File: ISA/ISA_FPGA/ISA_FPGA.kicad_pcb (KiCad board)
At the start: 2 copper layers, 44 parts, among them J1 Bus_ISA_16bit, J2 DE15, P1 CONN_5X2, P2 14.31818MHz, U1 74LVC245, U2 74LVC245, U3 74LVC245, U4 74LVC245, U5 74LVC245, U6 74LVC245, U7 CONN_30X2, U8 CONN_30X2, U9 74LVC06, X1 MINI_DIN_6, X2 MINI_DIN_6

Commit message: ISA - FPGA board
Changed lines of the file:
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@@
   (general
     (thickness 1.6)
-    (drawings 11)
+    (drawings 19)
     (tracks 0)
     (zones 0)
@@
       (net 79 /GND))
   )
+  (gr_line (start 274.828 32.766) (end 275.082 32.766) (layer F.SilkS) (width 0.12))
+  (gr_line (start 275.082 32.766) (end 275.082 32.766) (layer F.SilkS) (width 0.12))
+  (gr_line (start 88.646 32.512) (end 88.646 33.274) (layer F.SilkS) (width 0.12))
+  (gr_line (start 88.646 32.512) (end 88.646 32.512) (layer F.SilkS) (width 0.12))
+  (gr_line (start 88.9 152.4) (end 88.646 33.274) (layer F.SilkS) (width 0.12))
+  (gr_line (start 88.9 152.146) (end 105.664 152.146) (layer F.SilkS) (width 0.12))
+  (gr_line (start 105.41 152.146) (end 88.9 152.146) (layer F.SilkS) (width 0.12))
+  (gr_line (start 88.392 32.512) (end 88.646 33.02) (layer F.SilkS) (width 0.12))
+  (gr_line (start 274.828 32.766) (end 88.646 32.512) (layer F.SilkS) (width 0.12))
+  (gr_line (start 14.732 33.274) (end 14.224 33.274) (layer F.SilkS) (width 0.12))
+  (gr_line (start 88.9 152.4) (end 88.9 152.4) (layer F.SilkS) (width 0.12))
   (dimension 60.96 (width 0.12) (layer F.SilkS)
     (gr_text "60.960 mm" (at 172.72 39.37) (layer F.SilkS)
@@
     (arrow2b (pts (xy 203.2 38.1) (xy 202.073496 38.686421)))
   )
-  (gr_line (start 275.082 33.02) (end 14.224 33.274) (layer F.SilkS) (width 0.12))
-  (gr_line (start 14.478 152.4) (end 14.224 32.512) (layer F.SilkS) (width 0.12))
-  (gr_line (start 105.664 152.146) (end 14.478 152.4) (layer F.SilkS) (width 0.12))
   (gr_line (start 105.664 143.51) (end 105.664 152.146) (layer F.SilkS) (width 0.12))
   (gr_line (start 117.602 143.51) (end 105.664 143.51) (layer F.SilkS) (width 0.12))

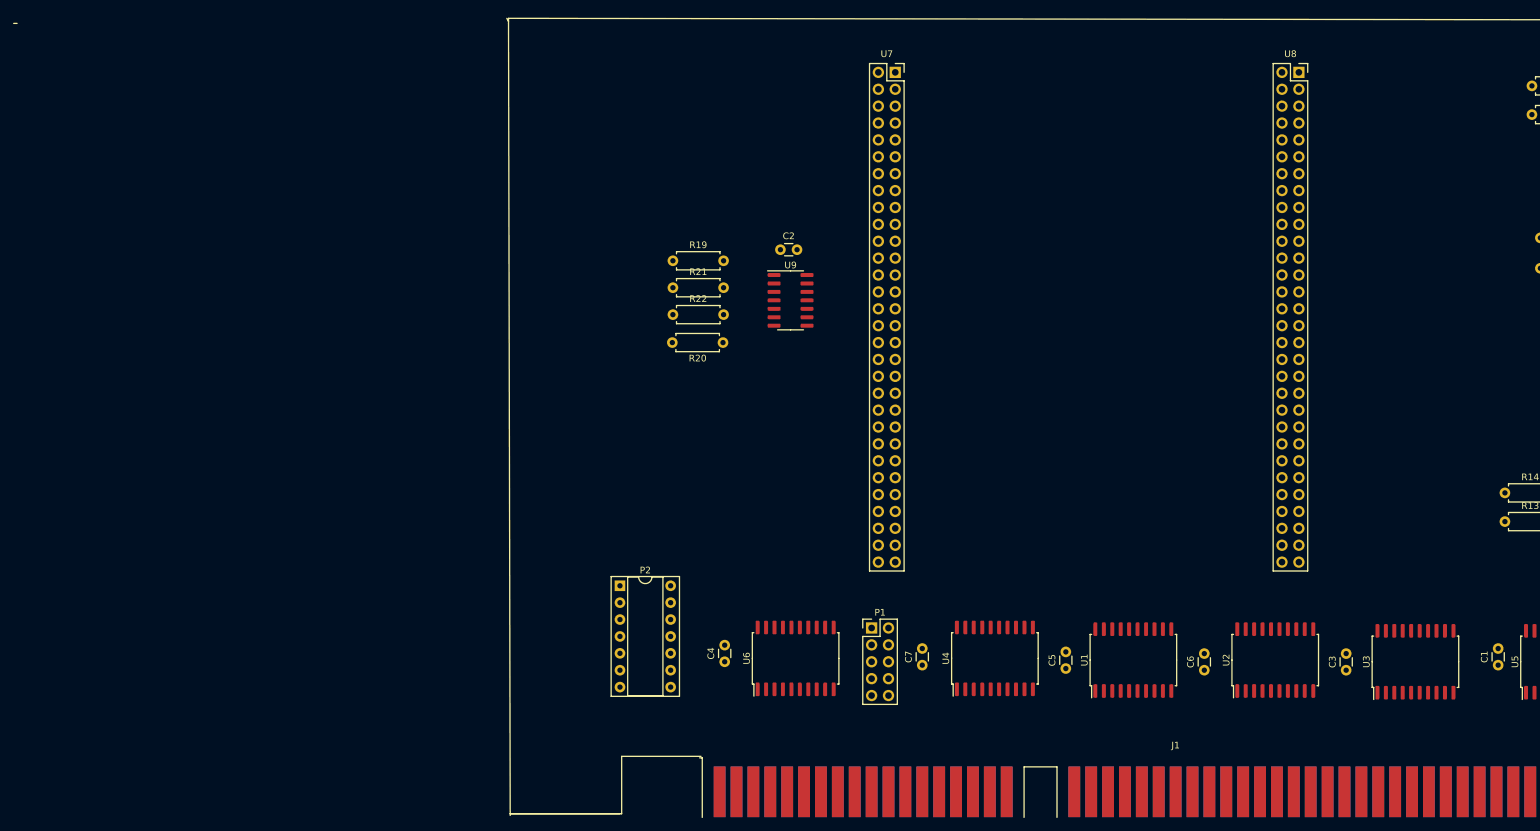
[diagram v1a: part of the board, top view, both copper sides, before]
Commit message: ISA - update
cad files for ISA video / cpu boards
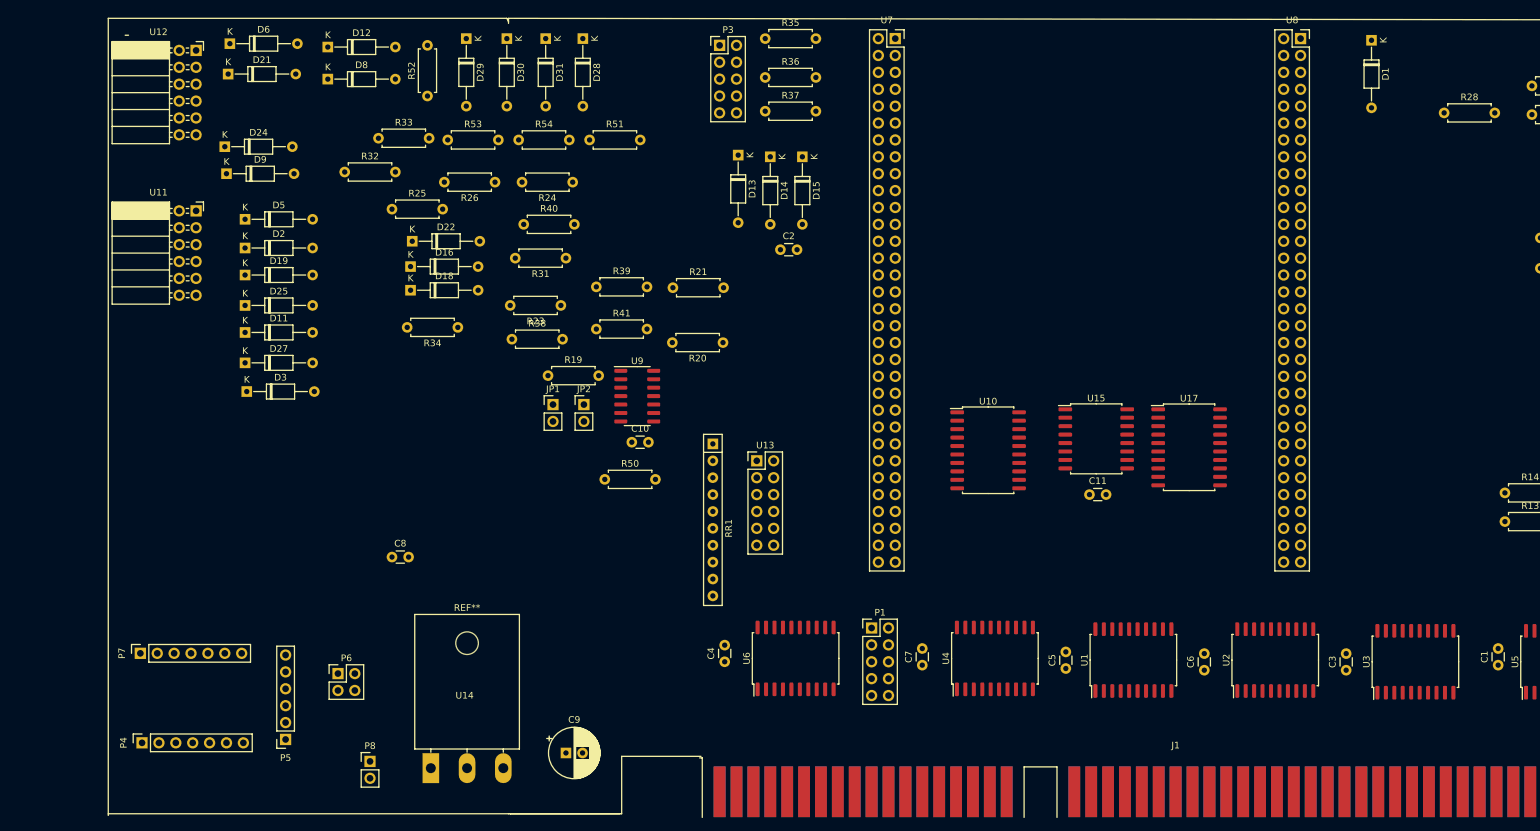
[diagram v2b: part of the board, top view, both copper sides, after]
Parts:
- removed P2: 14.31818MHz, Package_DIP:DIP-14_W7.62mm_Socket
- removed R22: 2k2, Resistor_THT:R_Axial_DIN0207_L6.3mm_D2.5mm_P7.62mm_Horizontal
- added C10: 0.1, Capacitor_THT:C_Disc_D3.0mm_W1.6mm_P2.50mm, F.Cu at (107.2, 96.3)
- added C11: 0.1, Capacitor_THT:C_Disc_D3.0mm_W1.6mm_P2.50mm, F.Cu at (176.0, 104.1)
- added C8: 0.1, Capacitor_THT:C_Disc_D3.0mm_W1.6mm_P2.50mm, F.Cu at (71.1, 113.5)
- added C9: 10uF, Capacitor_THT:CP_Radial_D7.5mm_P2.50mm, F.Cu at (97.3, 143.0)
- added D1: LED, Diode_THT:D_DO-35_SOD27_P10.16mm_Horizontal, F.Cu at (218.4, 35.8)
- added D11: ZPDxx, Diode_THT:D_DO-35_SOD27_P10.16mm_Horizontal, F.Cu at (49.0, 79.8)
- added D12: ZPDxx, Diode_THT:D_DO-35_SOD27_P10.16mm_Horizontal, F.Cu at (61.5, 36.8)
- added D13: ZPDxx, Diode_THT:D_DO-35_SOD27_P10.16mm_Horizontal, F.Cu at (123.2, 53.1)
- added D14: ZPDxx, Diode_THT:D_DO-35_SOD27_P10.16mm_Horizontal, F.Cu at (128.0, 53.3)
- added D15: ZPDxx, Diode_THT:D_DO-35_SOD27_P10.16mm_Horizontal, F.Cu at (132.8, 53.3)
- added D16: ZPDxx, Diode_THT:D_DO-35_SOD27_P10.16mm_Horizontal, F.Cu at (73.9, 69.8)
- added D18: ZPDxx, Diode_THT:D_DO-35_SOD27_P10.16mm_Horizontal, F.Cu at (73.9, 73.4)
- added D19: ZPDxx, Diode_THT:D_DO-35_SOD27_P10.16mm_Horizontal, F.Cu at (49.0, 71.1)
- added D2: ZPDxx, Diode_THT:D_DO-35_SOD27_P10.16mm_Horizontal, F.Cu at (49.0, 67.1)
- added D21: ZPDxx, Diode_THT:D_DO-35_SOD27_P10.16mm_Horizontal, F.Cu at (46.5, 40.9)
- added D22: ZPDxx, Diode_THT:D_DO-35_SOD27_P10.16mm_Horizontal, F.Cu at (74.2, 66.0)
- added D24: ZPDxx, Diode_THT:D_DO-35_SOD27_P10.16mm_Horizontal, F.Cu at (46.0, 51.8)
- added D25: ZPDxx, Diode_THT:D_DO-35_SOD27_P10.16mm_Horizontal, F.Cu at (49.0, 75.7)
- added D27: ZPDxx, Diode_THT:D_DO-35_SOD27_P10.16mm_Horizontal, F.Cu at (49.0, 84.3)
- added D28: LED, Diode_THT:D_DO-35_SOD27_P10.16mm_Horizontal, F.Cu at (99.8, 35.6)
- added D29: LED, Diode_THT:D_DO-35_SOD27_P10.16mm_Horizontal, F.Cu at (82.3, 35.6)
- added D3: ZPDxx, Diode_THT:D_DO-35_SOD27_P10.16mm_Horizontal, F.Cu at (49.3, 88.6)
- added D30: LED, Diode_THT:D_DO-35_SOD27_P10.16mm_Horizontal, F.Cu at (88.4, 35.6)
- added D31: LED, Diode_THT:D_DO-35_SOD27_P10.16mm_Horizontal, F.Cu at (94.2, 35.6)
- added D5: ZPDxx, Diode_THT:D_DO-35_SOD27_P10.16mm_Horizontal, F.Cu at (49.0, 62.7)
- added D6: ZPDxx, Diode_THT:D_DO-35_SOD27_P10.16mm_Horizontal, F.Cu at (46.7, 36.3)
- added D8: ZPDxx, Diode_THT:D_DO-35_SOD27_P10.16mm_Horizontal, F.Cu at (61.5, 41.7)
- added D9: ZPDxx, Diode_THT:D_DO-35_SOD27_P10.16mm_Horizontal, F.Cu at (46.2, 55.9)
- added JP1: Jumper, Connector_PinHeader_2.54mm:PinHeader_1x02_P2.54mm_Vertical, F.Cu at (95.3, 90.6)
- added JP2: Jumper, Connector_PinHeader_2.54mm:PinHeader_1x02_P2.54mm_Vertical, F.Cu at (100.0, 90.6)
- added P3: CONN_5X2, Connector_PinHeader_2.54mm:PinHeader_2x05_P2.54mm_Vertical, F.Cu at (120.4, 36.6)
- added P4: CONN_7, Connector_PinSocket_2.54mm:PinSocket_1x07_P2.54mm_Vertical, F.Cu at (33.5, 141.5)
- added P5: CONN_6, Connector_PinSocket_2.54mm:PinSocket_1x06_P2.54mm_Vertical, F.Cu at (55.1, 141.0)
- added P6: CONN_2X2, Connector_PinHeader_2.54mm:PinHeader_2x02_P2.54mm_Vertical, F.Cu at (63.0, 131.1)
- added P7: CONN_7, Connector_PinSocket_2.54mm:PinSocket_1x07_P2.54mm_Vertical, F.Cu at (33.3, 128.0)
- added P8: CONN_2, Connector_PinHeader_2.54mm:PinHeader_1x02_P2.54mm_Vertical, F.Cu at (67.8, 144.3)
- added R23: 200, Resistor_THT:R_Axial_DIN0207_L6.3mm_D2.5mm_P7.62mm_Horizontal, F.Cu at (96.5, 75.7)
- added R24: 200, Resistor_THT:R_Axial_DIN0207_L6.3mm_D2.5mm_P7.62mm_Horizontal, F.Cu at (98.3, 57.1)
- added R25: 200, Resistor_THT:R_Axial_DIN0207_L6.3mm_D2.5mm_P7.62mm_Horizontal, F.Cu at (71.1, 61.2)
- added R26: 200, Resistor_THT:R_Axial_DIN0207_L6.3mm_D2.5mm_P7.62mm_Horizontal, F.Cu at (86.6, 57.1)
- added R28: 100, Resistor_THT:R_Axial_DIN0207_L6.3mm_D2.5mm_P7.62mm_Horizontal, F.Cu at (229.4, 46.7)
- added R31: 200, Resistor_THT:R_Axial_DIN0207_L6.3mm_D2.5mm_P7.62mm_Horizontal, F.Cu at (97.3, 68.6)
- added R32: 200, Resistor_THT:R_Axial_DIN0207_L6.3mm_D2.5mm_P7.62mm_Horizontal, F.Cu at (64.0, 55.6)
- added R33: 200, Resistor_THT:R_Axial_DIN0207_L6.3mm_D2.5mm_P7.62mm_Horizontal, F.Cu at (69.1, 50.5)
- added R34: 200, Resistor_THT:R_Axial_DIN0207_L6.3mm_D2.5mm_P7.62mm_Horizontal, F.Cu at (81.0, 79.0)
- added R35: 100, Resistor_THT:R_Axial_DIN0207_L6.3mm_D2.5mm_P7.62mm_Horizontal, F.Cu at (127.3, 35.6)
- added R36: 100, Resistor_THT:R_Axial_DIN0207_L6.3mm_D2.5mm_P7.62mm_Horizontal, F.Cu at (127.3, 41.4)
- added R37: 100, Resistor_THT:R_Axial_DIN0207_L6.3mm_D2.5mm_P7.62mm_Horizontal, F.Cu at (127.3, 46.5)
- added R38: 200, Resistor_THT:R_Axial_DIN0207_L6.3mm_D2.5mm_P7.62mm_Horizontal, F.Cu at (89.2, 80.8)
- added R39: 200, Resistor_THT:R_Axial_DIN0207_L6.3mm_D2.5mm_P7.62mm_Horizontal, F.Cu at (101.9, 72.9)
- added R40: 200, Resistor_THT:R_Axial_DIN0207_L6.3mm_D2.5mm_P7.62mm_Horizontal, F.Cu at (90.9, 63.5)
- added R41: 200, Resistor_THT:R_Axial_DIN0207_L6.3mm_D2.5mm_P7.62mm_Horizontal, F.Cu at (101.9, 79.2)
- added R50: 10K, Resistor_THT:R_Axial_DIN0207_L6.3mm_D2.5mm_P7.62mm_Horizontal, F.Cu at (103.1, 101.9)
- added R51: 100, Resistor_THT:R_Axial_DIN0207_L6.3mm_D2.5mm_P7.62mm_Horizontal, F.Cu at (100.8, 50.8)
- added R52: 100, Resistor_THT:R_Axial_DIN0207_L6.3mm_D2.5mm_P7.62mm_Horizontal, F.Cu at (76.5, 44.2)
- added R53: 100, Resistor_THT:R_Axial_DIN0207_L6.3mm_D2.5mm_P7.62mm_Horizontal, F.Cu at (79.5, 50.8)
- added R54: 100, Resistor_THT:R_Axial_DIN0207_L6.3mm_D2.5mm_P7.62mm_Horizontal, F.Cu at (90.2, 50.8)
- added RR1: 10k, Resistor_THT:R_Array_SIP10, F.Cu at (119.4, 96.5)
- added U10: 74LVC245, Package_SO:SOIC-20W_7.5x12.8mm_P1.27mm, F.Cu at (160.8, 97.5)
- added U11: CONN_6x2, Connector_PinSocket_2.54mm:PinSocket_2x06_P2.54mm_Horizontal, F.Cu at (41.7, 61.5)
- added U12: CONN_6x2, Connector_PinSocket_2.54mm:PinSocket_2x06_P2.54mm_Horizontal, F.Cu at (41.7, 37.3)
- added U13: CONN_6x2, Connector_PinHeader_2.54mm:PinHeader_2x06_P2.54mm_Vertical, F.Cu at (126.0, 99.1)
- added U14: LM3940, Package_TO_SOT_THT:LMxx, F.Cu at (82.0, 133.9)
- added U15: 74LVC138, Package_SO:SOIC-16W_7.5x10.3mm_P1.27mm, F.Cu at (177.0, 95.8)
- added U17: 74LVC574, Package_SO:SOIC-20W_7.5x12.8mm_P1.27mm, F.Cu at (191.0, 97.0)
- U7, U8: value CONN_30X2 -> CONN_32X2; footprint Connector_PinSocket_2.54mm:PinSocket_2x30_P2.54mm_Vertical -> Connector_PinSocket_2.54mm:PinSocket_2x32_P2.54mm_Vertical
- moved U9 27.2 mm to (108.0, 89.3)
- moved R19 25.5 mm to (94.6, 86.3)
- moved U8 5.09 mm to (207.8, 35.6)
- moved U7 5.08 mm to (146.8, 35.6)
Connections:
- net /SEL0 renamed /A0
- net /SEL1 renamed /SBHE
- net Net-(J1-Pad2) renamed /RESET
- net Net-(U4-Pad13) renamed /8MH18Hz
- C1 pad 2: /GND -> GND
- C2 pad 2: /GND -> GND
- C3 pad 2: /GND -> GND
- C4 pad 2: /GND -> GND
- C5 pad 2: /GND -> GND
- C6 pad 2: /GND -> GND
- C7 pad 2: /GND -> GND
- J1 pad 1: /GND -> GND
- J1 pad 10: /GND -> GND
- J1 pad 15: Net-(J1-Pad15) -> /MAK3*
- J1 pad 16: Net-(J1-Pad16) -> /MRQ3
- J1 pad 17: Net-(J1-Pad17) -> /MAK1*
- J1 pad 18: Net-(J1-Pad18) -> /MRQ1
- J1 pad 26: Net-(J1-Pad26) -> /MAK2*
- J1 pad 29: /VCC -> VCC
- J1 pad 3: /VCC -> VCC
- J1 pad 30: /OSC -> Net-(J1-Pad30)
- J1 pad 31: /GND -> GND
- J1 pad 6: Net-(J1-Pad6) -> /MRQ2
- J1 pad 63: /CYC -> /MEMCS16*
- J1 pad 70: Net-(J1-Pad70) -> /MAK0*
- J1 pad 71: Net-(J1-Pad71) -> /MRQ0
- J1 pad 72: Net-(J1-Pad72) -> /MAK5*
- J1 pad 73: Net-(J1-Pad73) -> /MRQ5
- J1 pad 74: Net-(J1-Pad74) -> /MAK6*
- J1 pad 75: Net-(J1-Pad75) -> /MRQ6
- J1 pad 76: Net-(J1-Pad76) -> /MAK7*
- J1 pad 77: Net-(J1-Pad77) -> /MRQ7
- J1 pad 78: /VCC -> VCC
- J1 pad 80: /GND -> GND
- J1 pad 82: /A26 -> /A23
- J1 pad 83: /A25 -> /A22
- J1 pad 84: /A24 -> /A21
- J1 pad 85: /A23 -> /A20
- J1 pad 86: /A22 -> /A26
- J1 pad 87: /A21 -> /A25
- J1 pad 88: /A20 -> /A24
- J1 pad 89: Net-(J1-Pad89) -> /RD*
- J2 pad 10: /GND -> GND
- J2 pad 5: /GND -> GND
- J2 pad 6: /GND -> GND
- J2 pad 7: /GND -> GND
- J2 pad 8: /GND -> GND
- R19 pad 1: /FWR -> /MEMCS16*
- R19 pad 2: /VCC33 -> VCC
- R20 pad 2: /VCC -> VCC
- R21 pad 2: /VCC -> VCC
- U1 pad 10: /GND -> GND
- U1 pad 18: /FSEL0 -> /FA0
- U1 pad 19: /GND -> GND
- U2 pad 10: /GND -> GND
- U2 pad 19: /GND -> GND
- U3 pad 10: /GND -> GND
- U3 pad 19: /GND -> GND
- U4 pad 10: /GND -> GND
- U4 pad 11: Net-(U4-Pad11) -> /FWR*
- U4 pad 12: Net-(U4-Pad12) -> /14M318Hz
- U4 pad 14: /FSEL1 -> /FSBHE
- U4 pad 19: /GND -> GND
- U4 pad 7: Net-(U4-Pad7) -> /F8M18Hz
- U4 pad 8: Net-(U4-Pad8) -> /F14M318Hz
- U4 pad 9: Net-(U4-Pad9) -> /WR*
- U5 pad 1: /FWR -> /RD*
- U5 pad 10: /GND -> GND
- U6 pad 1: /FWR -> /RD*
- U6 pad 10: /GND -> GND
- U7 pad 1: /GND -> Net-(U7-Pad1)
- U7 pad 10: Net-(U7-Pad10) -> /FD6
- U7 pad 11: Net-(U7-Pad11) -> /PMODA2
- U7 pad 12: /FD4 -> /FD5
- U7 pad 13: Net-(U7-Pad13) -> /PMODA3
- U7 pad 14: /FD3 -> Net-(U7-Pad14)
- U7 pad 15: Net-(U7-Pad15) -> /PMODA4
- U7 pad 16: /FD2 -> /FD4
- U7 pad 17: Net-(U7-Pad17) -> /PMODA5
- U7 pad 18: /FD1 -> /FD3
- U7 pad 19: Net-(U7-Pad19) -> /PMODA6
- U7 pad 2: /GND -> Net-(U7-Pad2)
- U7 pad 20: /FD0 -> /FD2
- U7 pad 21: Net-(U7-Pad21) -> /PMODA7
- U7 pad 22: /FD15 -> /FD1
- U7 pad 23: Net-(U7-Pad23) -> /PMODB0
- U7 pad 24: /FD14 -> /FD0
- U7 pad 25: Net-(U7-Pad25) -> /PMODB1
- U7 pad 26: /FD13 -> /FD15
- U7 pad 27: Net-(U7-Pad27) -> /PMODB2
- U7 pad 28: /FD12 -> /FD14
- U7 pad 29: Net-(U7-Pad29) -> /ANA2
- U7 pad 30: /FD11 -> /ANA1
- U7 pad 31: Net-(U7-Pad31) -> /PMODB3
- U7 pad 32: /FD10 -> /FD13
- U7 pad 34: /FD9 -> /FD12
- U7 pad 35: Net-(U7-Pad35) -> /FMEMCS16
- U7 pad 36: /FD8 -> /FD11
- U7 pad 37: Net-(U7-Pad37) -> /F8M18Hz
- U7 pad 38: Net-(U7-Pad38) -> /FD10
- U7 pad 39: Net-(U7-Pad39) -> /F14M318Hz
- U7 pad 4: /FD7 -> Net-(U7-Pad4)
- U7 pad 40: Net-(U7-Pad40) -> /FD9
- U7 pad 41: Net-(U7-Pad41) -> /CFG4
- U7 pad 42: Net-(U7-Pad42) -> /FD8
- U7 pad 43: Net-(U7-Pad43) -> /FMRQ0
- U7 pad 44: Net-(U7-Pad44) -> /LED0
- U7 pad 45: Net-(U7-Pad45) -> /FMRQ1
- U7 pad 46: Net-(U7-Pad46) -> /LED1
- U7 pad 48: Net-(U7-Pad48) -> /LED2
- U7 pad 49: Net-(U7-Pad49) -> /FMRQ2
- U7 pad 5: Net-(U7-Pad5) -> GND
- U7 pad 50: Net-(U7-Pad50) -> /LED3
- U7 pad 52: Net-(U7-Pad52) -> /CFG3
- U7 pad 53: Net-(U7-Pad53) -> /FMRQ3
- U7 pad 54: Net-(U7-Pad54) -> /MS0
- U7 pad 55: Net-(U7-Pad55) -> /FMRQ5
- U7 pad 56: Net-(U7-Pad56) -> /MS1
- U7 pad 57: /GND -> /FMRQ6
- U7 pad 58: /GND -> /MS2
- U7 pad 59: /VCC -> /FMRQ7
- U7 pad 6: /FD6 -> GND
- U7 pad 60: /VCC -> /CFG2
- U7 pad 7: Net-(U7-Pad7) -> /PMODA0
- U7 pad 8: /FD5 -> /FD7
- U7 pad 9: Net-(U7-Pad9) -> /PMODA1
- U8 pad 1: /GND -> Net-(U8-Pad1)
- U8 pad 10: Net-(U8-Pad10) -> /KBDCLK
- U8 pad 11: /FA4 -> /FA2
- U8 pad 12: /MSECLK -> /MSEDAT
- U8 pad 13: /FA5 -> /FA3
- U8 pad 14: /FALE -> /FA4
- U8 pad 15: /FA6 -> /ANA0
- U8 pad 16: /FWR -> /MSECLK
- U8 pad 17: /FA7 -> /FA5
- U8 pad 18: /RDY* -> /FALE
- U8 pad 19: /FA8 -> /FA6
- U8 pad 2: /GND -> Net-(U8-Pad2)
- U8 pad 20: /FDBE* -> /FWR*
- U8 pad 21: /FA9 -> /FA7
- U8 pad 22: /IRQ -> /RDY*
- U8 pad 23: /FA10 -> /FA8
- U8 pad 24: Net-(U8-Pad24) -> /FDBE*
- U8 pad 25: /FA11 -> /FA9
- U8 pad 26: Net-(U8-Pad26) -> /IRQ
- U8 pad 27: /FA12 -> /FA10
- U8 pad 28: Net-(U8-Pad28) -> /FTX
- U8 pad 29: /FA13 -> /FA11
- U8 pad 3: /FA0 -> Net-(U8-Pad3)
- U8 pad 30: /BLUE3 -> /FRX
- U8 pad 31: /FA14 -> /FA12
- U8 pad 32: /BLUE2 -> /FSBHE
- U8 pad 33: /FA15 -> /FA13
- U8 pad 34: /BLUE1 -> /BLUE3
- U8 pad 35: /FA23 -> /FA14
- U8 pad 36: /BLUE0 -> /BLUE2
- U8 pad 37: /FA22 -> /FA15
- U8 pad 38: /GREEN3 -> /BLUE1
- U8 pad 39: /FA21 -> /FA23
- U8 pad 4: /KBDDAT -> Net-(U8-Pad4)
- U8 pad 40: /GREEN2 -> /BLUE0
- U8 pad 41: /FA20 -> /FA22
- U8 pad 42: /GREEN1 -> /GREEN3
- U8 pad 43: /FA19 -> /FA21
- U8 pad 44: /GREEN0 -> /GREEN2
- U8 pad 45: /FA18 -> /FA20
- U8 pad 46: /RED3 -> /GREEN1
- U8 pad 47: /FA17 -> /FA19
- U8 pad 48: /RED2 -> /GREEN0
- U8 pad 49: /FA16 -> /FA18
- U8 pad 5: /FA1 -> GND
- U8 pad 50: /RED1 -> /RED3
- U8 pad 51: /FA24 -> /FA17
- U8 pad 52: /RED0 -> /RED2
- U8 pad 53: /FA25 -> /FA16
- U8 pad 54: /VS -> /RED1
- U8 pad 55: /FA26 -> /FA24
- U8 pad 56: /HS -> /RED0
- U8 pad 57: /GND -> /FA25
- U8 pad 58: /GND -> /VS
- U8 pad 59: /VCC -> /FA26
- U8 pad 6: /KBDCLK -> GND
- U8 pad 60: /VCC -> /HS
- U8 pad 7: /FA2 -> /FA0
- U8 pad 8: /MSEDAT -> /KBDDAT
- U8 pad 9: /FA3 -> /FA1
- U9 pad 1: /WR* -> (no net)
- U9 pad 10: (no net) -> /MEMCS16*
- U9 pad 11: (no net) -> /FMEMCS16
- U9 pad 14: (no net) -> /VCC33
- U9 pad 2: /FWR -> (no net)
- U9 pad 3: Net-(P2-Pad10) -> (no net)
- U9 pad 4: /OSC -> (no net)
- U9 pad 7: (no net) -> GND

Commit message: Petajon - update
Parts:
- removed D11, D12, D16, D18, D19, D2, D21, D22, D24, D25, D27, D3, D5, D6, D8, D9: ZPDxx, Diode_THT:D_DO-35_SOD27_P10.16mm_Horizontal
- removed R25, R26, R31, R32, R33, R34, R38, R39, R40, R41: 200, Resistor_THT:R_Axial_DIN0207_L6.3mm_D2.5mm_P7.62mm_Horizontal
- added C12: 0.047u, Capacitor_THT:C_Disc_D3.8mm_W2.6mm_P2.50mm, F.Cu at (215.6, 82.8)
- added C13: 10u, Capacitor_THT:CP_Radial_D5.0mm_P2.50mm, F.Cu at (238.0, 56.9)
- added C14: 100u, Capacitor_THT:CP_Radial_D8.0mm_P3.80mm, F.Cu at (224.5, 72.6)
- added C15: 0.047u, Capacitor_THT:C_Disc_D5.0mm_W2.5mm_P5.00mm, F.Cu at (223.8, 89.2)
- added C16: 220u, Capacitor_THT:CP_Radial_D8.0mm_P3.80mm, F.Cu at (231.6, 72.6)
- added C17: 0.1, Capacitor_THT:C_Disc_D3.0mm_W1.6mm_P2.50mm, F.Cu at (175.5, 115.3)
- added C18: 0.1, Capacitor_THT:C_Disc_D3.0mm_W1.6mm_P2.50mm, F.Cu at (159.8, 115.1)
- added C19: 0.1, Capacitor_THT:C_Disc_D3.0mm_W1.6mm_P2.50mm, F.Cu at (191.3, 115.3)
- added C20: 0.1, Capacitor_THT:C_Disc_D3.0mm_W1.6mm_P2.50mm, F.Cu at (77.0, 38.6)
- added C21: 0.1, Capacitor_THT:C_Disc_D3.0mm_W1.6mm_P2.50mm, F.Cu at (75.2, 58.7)
- added C22: 0.1, Capacitor_THT:C_Disc_D3.0mm_W1.6mm_P2.50mm, F.Cu at (75.2, 79.0)
- added C23: 0.1, Capacitor_THT:C_Disc_D3.0mm_W1.6mm_P2.50mm, F.Cu at (90.9, 71.9)
- added C24: 0.1, Capacitor_THT:C_Disc_D3.0mm_W1.6mm_P2.50mm, F.Cu at (188.2, 95.0)
- added J3: AudioJack2, Connector_Audio:Jack_3.5mm_CUI_SJ1-3533NG_Horizontal, F.Cu at (274.8, 128.8)
- added P2: CONN_2, Connector_PinHeader_2.54mm:PinHeader_1x02_P2.54mm_Vertical, F.Cu at (107.2, 77.5)
- added R22: 10k, Resistor_THT:R_Axial_DIN0207_L6.3mm_D2.5mm_P7.62mm_Horizontal, F.Cu at (87.9, 81.5)
- added R27: 5k1, Resistor_THT:R_Axial_DIN0207_L6.3mm_D2.5mm_P7.62mm_Horizontal, F.Cu at (214.1, 70.1)
- added R29: 5k1, Resistor_THT:R_Axial_DIN0207_L6.3mm_D2.5mm_P7.62mm_Horizontal, F.Cu at (216.9, 55.1)
- added R30: 10, Resistor_THT:R_Axial_DIN0207_L6.3mm_D2.5mm_P7.62mm_Horizontal, F.Cu at (223.8, 81.5)
- added U16: LM386, Package_DIP:DIP-8_W7.62mm_Socket, F.Cu at (223.8, 54.9)
- added U18: 74LVC257, Package_SO:SOIC-16W_7.5x10.3mm_P1.27mm, F.Cu at (192.8, 106.4)
- added U19: CONN_20X2, Connector_PinHeader_2.54mm:PinHeader_2x20_P2.54mm_Horizontal, F.Cu at (58.2, 93.0)
- added U20: 74LVC573, Package_SO:SOIC-20W_7.5x12.8mm_P1.27mm, F.Cu at (109.5, 62.7)
- added U21: 74LVC245, Package_SO:SOIC-20W_7.5x12.8mm_P1.27mm, F.Cu at (76.7, 68.1)
- added U22: 74LVC245, Package_SO:SOIC-20W_7.5x12.8mm_P1.27mm, F.Cu at (76.7, 89.2)
- R19: value 2k2 -> 10k
- R23, R24: value 200 -> 10k
- U11: value CONN_6x2 -> 74LVC244; footprint Connector_PinSocket_2.54mm:PinSocket_2x06_P2.54mm_Horizontal -> Package_SO:SOIC-20W_7.5x12.8mm_P1.27mm
- U12: value CONN_6x2 -> 74LVC257; footprint Connector_PinSocket_2.54mm:PinSocket_2x06_P2.54mm_Horizontal -> Package_SO:SOIC-16W_7.5x10.3mm_P1.27mm
- U4: value 74LVC245 -> 74LVC257; footprint Package_SO:SOIC-20W_7.5x12.8mm_P1.27mm -> Package_SO:SOIC-16W_7.5x10.3mm_P1.27mm
- moved U12 151.4 mm to (176.5, 106.2)
- moved P8 49.3 mm to (106.9, 114.3)
- moved U11 36.3 mm to (75.4, 48.3)
- moved P6 36.2 mm to (90.2, 107.2)
- moved R24 35.7 mm to (87.6, 91.2), turned to 0 degrees
- moved P4 33.6 mm to (56.6, 117.1)
- moved P5 33.6 mm to (78.2, 116.6)
- moved P7 33.6 mm to (56.4, 103.6)
- moved U4 22.6 mm to (160.8, 106.2), turned to 0 degrees
- moved C8 19.7 mm to (86.6, 101.3)
- moved R52 14.8 mm to (91.2, 43.4)
- moved D28 14.8 mm to (114.6, 34.8)
- moved D29 14.8 mm to (97.0, 34.8)
- moved D30 14.8 mm to (103.1, 34.8)
- moved D31 14.8 mm to (109.0, 34.8)
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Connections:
- net /A0 renamed /AD16
- net /A1 renamed /AD17
- net /A10 renamed /AD26
- net /A11 renamed /AD27
- net /A12 renamed /AD28
- net /A13 renamed /AD29
- net /A14 renamed /AD30
- net /A15 renamed /AD31
- net /A2 renamed /AD18
- net /A3 renamed /AD19
- net /A4 renamed /AD20
- net /A5 renamed /AD21
- net /A6 renamed /AD22
- net /A7 renamed /AD23
- net /A8 renamed /AD24
- net /A9 renamed /AD25
- net /D0 renamed /AD0
- net /D1 renamed /AD1
- net /D10 renamed /AD10
- net /D11 renamed /AD11
- net /D12 renamed /AD12
- net /D13 renamed /AD13
- net /D14 renamed /AD14
- net /D15 renamed /AD15
- net /D2 renamed /AD2
- net /D3 renamed /AD3
- net /D4 renamed /AD4
- net /D5 renamed /AD5
- net /D6 renamed /AD6
- net /D7 renamed /AD7
- net /D8 renamed /AD8
- net /D9 renamed /AD9
- net /FA0 renamed /FAD16
- net /FA1 renamed /FAD17
- net /FA10 renamed /FAD26
- net /FA11 renamed /FAD27
- net /FA12 renamed /FAD28
- net /FA13 renamed /FAD29
- net /FA14 renamed /FAD30
- net /FA15 renamed /FAD31
- net /FA2 renamed /FAD18
- net /FA3 renamed /FAD19
- net /FA4 renamed /FAD20
- net /FA5 renamed /FAD21
- net /FA6 renamed /FAD22
- net /FA7 renamed /FAD23
- net /FA8 renamed /FAD24
- net /FA9 renamed /FAD25
- net /FD0 renamed /FAD0
- net /FD1 renamed /FAD1
- net /FD10 renamed /FAD10
- net /FD11 renamed /FAD11
- net /FD12 renamed /FAD12
- net /FD13 renamed /FAD13
- net /FD14 renamed /FAD14
- net /FD15 renamed /FAD15
- net /FD2 renamed /FAD2
- net /FD3 renamed /FAD3
- net /FD4 renamed /FAD4
- net /FD5 renamed /FAD5
- net /FD6 renamed /FAD6
- net /FD7 renamed /FAD7
- net /FD8 renamed /FAD8
- net /FD9 renamed /FAD9
- net Net-(J1-Pad67) renamed /IRQ12
- net Net-(J1-Pad68) renamed /IRQ15
- J1 pad 21: Net-(J1-Pad21) -> /IRQ7
- J1 pad 22: Net-(J1-Pad22) -> /IRQ6
- J1 pad 23: Net-(J1-Pad23) -> /IRQ5
- J1 pad 24: Net-(J1-Pad24) -> /IRQ4
- J1 pad 25: Net-(J1-Pad25) -> /IRQ3
- J1 pad 4: Net-(J1-Pad4) -> /IRQ2
- J1 pad 43: /A19 -> /SEL3
- J1 pad 44: /A18 -> /SEL2
- J1 pad 45: /A17 -> /SEL1
- J1 pad 46: /A16 -> /SEL0
- J1 pad 63: /MEMCS16* -> Net-(J1-Pad63)
- J1 pad 65: Net-(J1-Pad65) -> /IRQ10
- J1 pad 66: Net-(J1-Pad66) -> /IRQ11
- J1 pad 81: /SBHE -> Net-(J1-Pad81)
- J1 pad 82: /A23 -> Net-(J1-Pad82)
- J1 pad 83: /A22 -> Net-(J1-Pad83)
- J1 pad 84: /A21 -> Net-(J1-Pad84)
- J1 pad 85: /A20 -> Net-(J1-Pad85)
- J1 pad 86: /A26 -> Net-(J1-Pad86)
- J1 pad 87: /A25 -> Net-(J1-Pad87)
- J1 pad 88: /A24 -> Net-(J1-Pad88)
- J1 pad 89: /RD* -> Net-(J1-Pad89)
- J1 pad 9: Net-(J1-Pad9) -> /+12V
- J1 pad 90: /WR* -> /RD
- P1 pad 10: Net-(J1-Pad69) -> Net-(P1-Pad10)
- P1 pad 2: Net-(J1-Pad65) -> /IRQ10
- P1 pad 4: Net-(J1-Pad66) -> /IRQ11
- R19 pad 1: /MEMCS16* -> /DD7
- R19 pad 2: VCC -> GND
- R23 pad 1: /PMODA0 -> /DIORDY
- R23 pad 2: Net-(D11-Pad1) -> GND
- R24 pad 1: /PMODA1 -> /CSEL
- R24 pad 2: Net-(D8-Pad1) -> GND
- RR1 pad 2: Net-(RR1-Pad2) -> /CFG0
- RR1 pad 3: Net-(RR1-Pad3) -> /CFG1
- U1 pad 1: /VCC33 -> /FBDIR
- U1 pad 19: GND -> /FBEN
- U10 pad 11: Net-(U10-Pad11) -> /DMARQ
- U10 pad 9: Net-(U10-Pad9) -> /DDMARQ
- U11 pad 1: Net-(D11-Pad1) -> GND
- U11 pad 11: /VCC33 -> Net-(U11-Pad11)
- U11 pad 12: /VCC33 -> /CS3FX*
- U11 pad 2: Net-(D25-Pad1) -> /FDIOW*
- U11 pad 3: Net-(D8-Pad1) -> Net-(U11-Pad3)
- U11 pad 4: Net-(D22-Pad1) -> /FDIOR*
- U11 pad 6: Net-(D16-Pad1) -> /FCS1FX*
- U11 pad 8: Net-(D19-Pad1) -> /FCS3FX*
- U11 pad 9: GND -> Net-(U11-Pad9)
- U12 pad 1: Net-(D12-Pad1) -> /FIRQS
- U12 pad 10: GND -> Net-(U12-Pad10)
- U12 pad 11: /VCC33 -> /IRQ11
- U12 pad 12: /VCC33 -> /FIRQ6
- U12 pad 2: Net-(D27-Pad1) -> /IRQ6
- U12 pad 3: Net-(D9-Pad1) -> /CFG4
- U12 pad 4: Net-(D24-Pad1) -> /FIRQ4
- U12 pad 5: Net-(D6-Pad1) -> /IRQ7
- U12 pad 7: Net-(D3-Pad1) -> /FIRQ5
- U12 pad 8: Net-(D18-Pad1) -> GND
- U12 pad 9: GND -> /FIRQ7
- U13 pad 1: Net-(RR1-Pad2) -> /CFG0
- U13 pad 3: Net-(RR1-Pad3) -> /CFG1
- U17 pad 12: /MAK7* -> Net-(U17-Pad12)
- U17 pad 13: /MAK6* -> /MAK7*
- U17 pad 14: /MAK5* -> /MAK6*
- U17 pad 15: /MAK3* -> /MAK5*
- U17 pad 16: /MAK2* -> /MAK3*
- U17 pad 17: /MAK1* -> /MAK2*
- U17 pad 18: /MAK0* -> /MAK1*
- U17 pad 19: Net-(U17-Pad19) -> /MAK0*
- U17 pad 20: Net-(U17-Pad20) -> /VCC33
- U2 pad 1: /VCC33 -> /FBDIR
- U2 pad 19: GND -> /FBEN
- U3 pad 1: /VCC33 -> /FCDIR
- U3 pad 11: /FA23 -> /F14M318Hz
- U3 pad 12: /FA22 -> /F8M18Hz
- U3 pad 13: /FA21 -> /FRD
- U3 pad 14: /FA20 -> /FALE
- U3 pad 15: /FA19 -> /FSEL0
- U3 pad 16: /FA18 -> /FSEL1
- U3 pad 17: /FA17 -> /FSEL2
- U3 pad 18: /FA16 -> /FSEL3
- U3 pad 19: GND -> /FBEN
- U3 pad 2: /A16 -> /SEL3
- U3 pad 3: /A17 -> /SEL2
- U3 pad 4: /A18 -> /SEL1
- U3 pad 5: /A19 -> /SEL0
- U3 pad 6: /A20 -> /ALE
- U3 pad 7: /A21 -> /RD
- U3 pad 8: /A22 -> /8M18Hz
- U3 pad 9: /A23 -> /14M318Hz
- U4 pad 1: /VCC33 -> /FIRQS
- U4 pad 10: GND -> /CFG3
- U4 pad 11: /FWR* -> /IRQ5
- U4 pad 12: /14M318Hz -> /FIRQ2
- U4 pad 13: /8MH18Hz -> /CFG2
- U4 pad 14: /FSBHE -> /IRQ4
- U4 pad 15: /FALE -> GND
- U4 pad 16: /FA26 -> /VCC33
- U4 pad 2: /A24 -> /IRQ2
- U4 pad 3: /A25 -> /CFG0
- U4 pad 4: /A26 -> /FIRQ0
- U4 pad 5: /ALE -> /IRQ3
- U4 pad 6: /SBHE -> /CFG1
- U4 pad 7: /F8M18Hz -> /FIRQ1
- U4 pad 8: /F14M318Hz -> GND
- U4 pad 9: /WR* -> /FIRQ3
- U5 pad 1: /RD* -> /FBDIR
- U5 pad 19: /FDBE* -> /FBEN
- U6 pad 1: /RD* -> /FBDIR
- U6 pad 19: /FDBE* -> /FBEN
- U7 pad 1: Net-(U7-Pad1) -> GND
- U7 pad 11: /PMODA2 -> /FCS1FX*
- U7 pad 13: /PMODA3 -> /FCS3FX*
- U7 pad 15: /PMODA4 -> /DRDY*
- U7 pad 17: /PMODA5 -> /DDIR
- U7 pad 19: /PMODA6 -> /DBEN*
- U7 pad 2: Net-(U7-Pad2) -> GND
- U7 pad 21: /PMODA7 -> /RESET*
- U7 pad 23: /PMODB0 -> /FIRQ0
- U7 pad 25: /PMODB1 -> /FIRQ1
- U7 pad 27: /PMODB2 -> /FIRQ2
- U7 pad 31: /PMODB3 -> /FIRQ3
- U7 pad 35: /FMEMCS16 -> /FIRQ10
- U7 pad 41: /CFG4 -> /DDMARQ
- U7 pad 52: /CFG3 -> /AUD
- U7 pad 60: /CFG2 -> /FIRQ4
- U7 pad 7: /PMODA0 -> /FDIOW*
- U7 pad 9: /PMODA1 -> /FDIOR*
- U8 pad 1: Net-(U8-Pad1) -> GND
- U8 pad 2: Net-(U8-Pad2) -> GND
- U8 pad 20: /FWR* -> /FRD
- U8 pad 24: /FDBE* -> /FBDIR
- U8 pad 26: /IRQ -> /FIRQS
- U8 pad 32: /FSBHE -> /FCDIR
- U8 pad 39: /FA23 -> /FSEL0
- U8 pad 41: /FA22 -> /FSEL1
- U8 pad 43: /FA21 -> /FSEL2
- U8 pad 45: /FA20 -> /FSEL3
- U8 pad 47: /FA19 -> /FRDY*
- U8 pad 49: /FA18 -> /FBEN
- U8 pad 51: /FA17 -> /FIRQ5
- U8 pad 53: /FA16 -> /FIRQ6
- U8 pad 55: /FA24 -> /FIRQ7
- U8 pad 57: /FA25 -> /FIRQ8
- U8 pad 59: /FA26 -> /FIRQ9
- U9 pad 1: (no net) -> /RDY
- U9 pad 10: /MEMCS16* -> /DRDY*
- U9 pad 11: /FMEMCS16 -> /DIORDY
- U9 pad 2: (no net) -> /FRDY*
- U9 pad 3: (no net) -> /RESET
- U9 pad 4: (no net) -> /RESET*
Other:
- board text added: "(c) 2020 Finitron"
